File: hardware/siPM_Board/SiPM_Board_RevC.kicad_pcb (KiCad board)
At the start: 4 copper layers, 50.6 x 50.6 mm, 24 parts, among them J1 Conn_02x34_Odd_Even, J2 Conn_02x34_Odd_Even, U1 LM94021, U2 S14161-6050HS-04, U3 S14161-6050HS-04, U4 S14161-6050HS-04, U5 S14161-6050HS-04

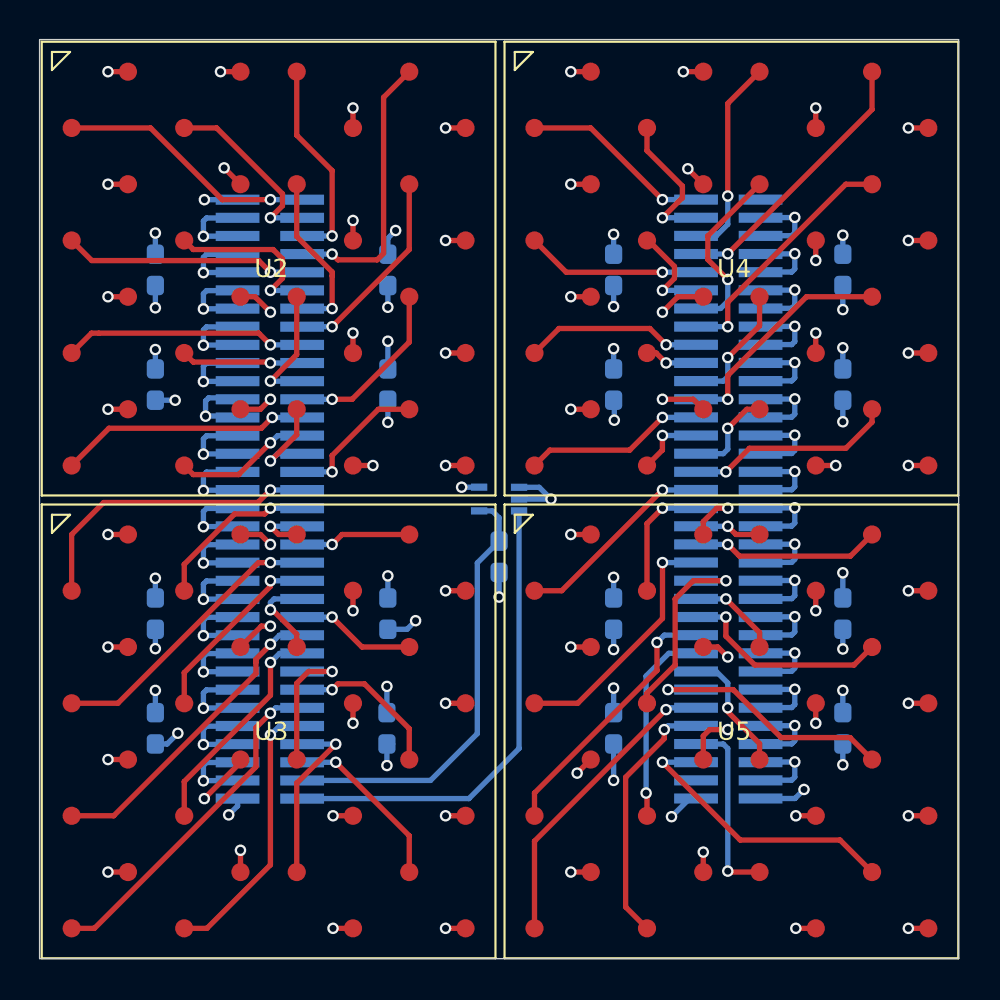
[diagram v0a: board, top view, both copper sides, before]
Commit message: SiPM Board RevC updated
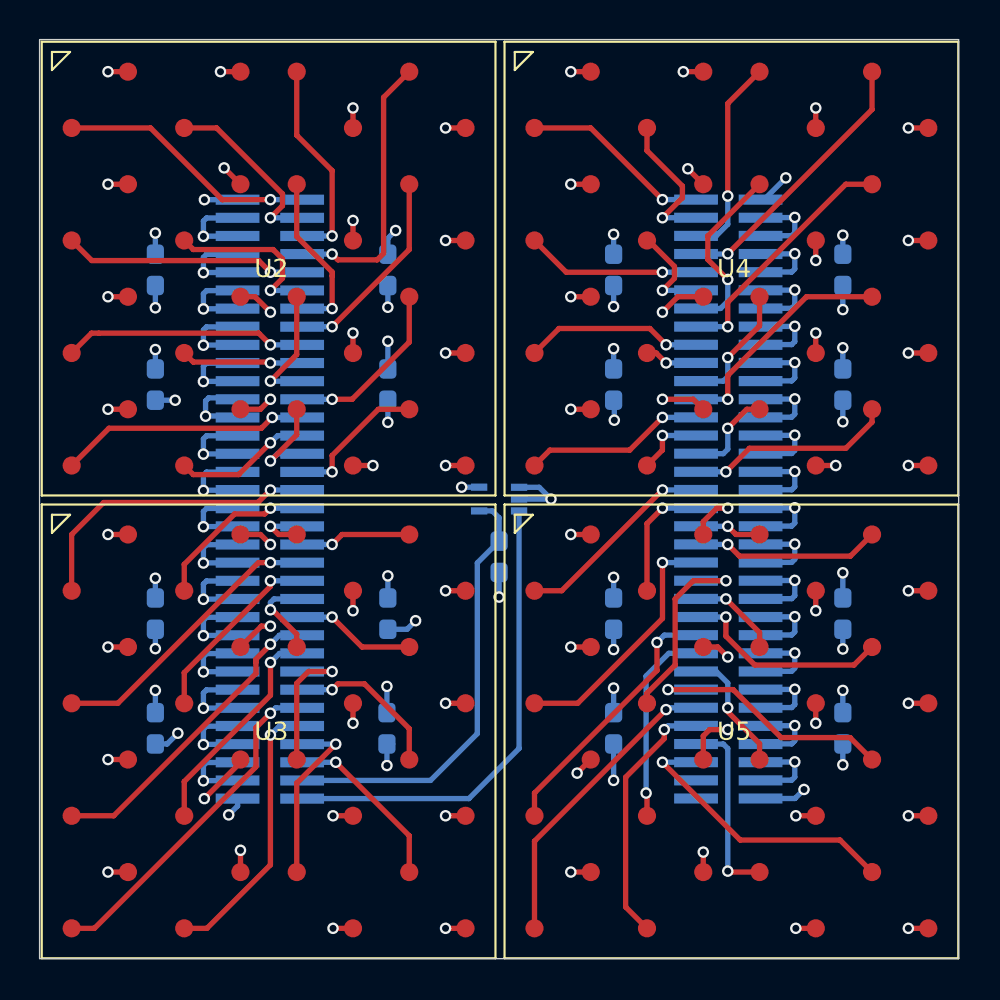
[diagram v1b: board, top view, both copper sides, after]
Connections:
- J2 pad 1: /BIAS4 -> Net-(J2-Pad1)
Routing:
- net /BIAS3: track 25.7 -> 27.6 mm, vias 20 -> 21
- net /BIAS4: track 30.5 -> 28.7 mm, vias 22 -> 21

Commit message: SiPM Board RevC modified
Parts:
- turned J2 to 270 degrees
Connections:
- J2 pad 1: Net-(J2-Pad1) -> /BIAS3
- J2 pad 10: GND -> Net-(J2-Pad10)
- J2 pad 11: Net-(J2-Pad11) -> GND
- J2 pad 12: GND -> Net-(J2-Pad12)
- J2 pad 13: Net-(J2-Pad13) -> GND
- J2 pad 14: GND -> Net-(J2-Pad14)
- J2 pad 15: Net-(J2-Pad15) -> GND
- J2 pad 16: GND -> Net-(J2-Pad16)
- J2 pad 17: Net-(J2-Pad17) -> GND
- J2 pad 18: GND -> Net-(J2-Pad18)
- J2 pad 19: Net-(J2-Pad19) -> GND
- J2 pad 2: /BIAS4 -> Net-(J2-Pad2)
- J2 pad 20: GND -> Net-(J2-Pad20)
- J2 pad 21: Net-(J2-Pad21) -> GND
- J2 pad 22: GND -> Net-(J2-Pad22)
- J2 pad 23: Net-(J2-Pad23) -> GND
- J2 pad 24: GND -> Net-(J2-Pad24)
- J2 pad 25: Net-(J2-Pad25) -> GND
- J2 pad 26: GND -> Net-(J2-Pad26)
- J2 pad 27: Net-(J2-Pad27) -> GND
- J2 pad 28: GND -> Net-(J2-Pad28)
- J2 pad 29: Net-(J2-Pad29) -> GND
- J2 pad 3: Net-(J2-Pad3) -> GND
- J2 pad 30: GND -> Net-(J2-Pad30)
- J2 pad 31: Net-(J2-Pad31) -> GND
- J2 pad 32: GND -> Net-(J2-Pad32)
- J2 pad 33: Net-(J2-Pad33) -> GND
- J2 pad 34: GND -> Net-(J2-Pad34)
- J2 pad 35: Net-(J2-Pad35) -> GND
- J2 pad 36: GND -> Net-(J2-Pad36)
- J2 pad 37: Net-(J2-Pad37) -> GND
- J2 pad 38: GND -> Net-(J2-Pad38)
- J2 pad 39: Net-(J2-Pad39) -> GND
- J2 pad 4: GND -> Net-(J2-Pad4)
- J2 pad 40: GND -> Net-(J2-Pad40)
- J2 pad 41: Net-(J2-Pad41) -> GND
- J2 pad 42: GND -> Net-(J2-Pad42)
- J2 pad 43: Net-(J2-Pad43) -> GND
- J2 pad 44: GND -> Net-(J2-Pad44)
- J2 pad 45: Net-(J2-Pad45) -> GND
- J2 pad 46: GND -> Net-(J2-Pad46)
- J2 pad 47: Net-(J2-Pad47) -> GND
- J2 pad 48: GND -> Net-(J2-Pad48)
- J2 pad 49: Net-(J2-Pad49) -> GND
- J2 pad 5: Net-(J2-Pad5) -> GND
- J2 pad 50: GND -> Net-(J2-Pad50)
- J2 pad 51: Net-(J2-Pad51) -> GND
- J2 pad 52: GND -> Net-(J2-Pad52)
- J2 pad 53: Net-(J2-Pad53) -> GND
- J2 pad 54: GND -> Net-(J2-Pad54)
- J2 pad 55: Net-(J2-Pad55) -> GND
- J2 pad 56: GND -> Net-(J2-Pad56)
- J2 pad 57: Net-(J2-Pad57) -> GND
- J2 pad 58: GND -> Net-(J2-Pad58)
- J2 pad 59: Net-(J2-Pad59) -> GND
- J2 pad 6: GND -> Net-(J2-Pad6)
- J2 pad 60: GND -> Net-(J2-Pad60)
- J2 pad 61: Net-(J2-Pad61) -> GND
- J2 pad 62: GND -> Net-(J2-Pad62)
- J2 pad 63: Net-(J2-Pad63) -> GND
- J2 pad 64: GND -> Net-(J2-Pad64)
- J2 pad 65: Net-(J2-Pad65) -> GND
- J2 pad 66: GND -> Net-(J2-Pad66)
- J2 pad 67: Net-(J2-Pad67) -> /BIAS4
- J2 pad 68: /BIAS3 -> Net-(J2-Pad68)
- J2 pad 7: Net-(J2-Pad7) -> GND
- J2 pad 8: GND -> Net-(J2-Pad8)
- J2 pad 9: Net-(J2-Pad9) -> GND
- U4 pad A2: Net-(J2-Pad67) -> Net-(J2-Pad2)
- U4 pad A4: Net-(J2-Pad59) -> Net-(J2-Pad10)
- U4 pad A6: Net-(J2-Pad51) -> Net-(J2-Pad18)
- U4 pad A8: Net-(J2-Pad43) -> Net-(J2-Pad26)
- U4 pad C2: Net-(J2-Pad65) -> Net-(J2-Pad4)
- U4 pad C4: Net-(J2-Pad57) -> Net-(J2-Pad12)
- U4 pad C6: Net-(J2-Pad49) -> Net-(J2-Pad20)
- U4 pad C8: Net-(J2-Pad41) -> Net-(J2-Pad28)
- U4 pad E1: Net-(J2-Pad63) -> Net-(J2-Pad6)
- U4 pad E3: Net-(J2-Pad55) -> Net-(J2-Pad14)
- U4 pad E5: Net-(J2-Pad47) -> Net-(J2-Pad22)
- U4 pad E7: Net-(J2-Pad39) -> Net-(J2-Pad30)
- U4 pad G1: Net-(J2-Pad61) -> Net-(J2-Pad8)
- U4 pad G3: Net-(J2-Pad53) -> Net-(J2-Pad16)
- U4 pad G5: Net-(J2-Pad45) -> Net-(J2-Pad24)
- U4 pad G7: Net-(J2-Pad37) -> Net-(J2-Pad32)
- U5 pad A2: Net-(J2-Pad35) -> Net-(J2-Pad34)
- U5 pad A4: Net-(J2-Pad27) -> Net-(J2-Pad42)
- U5 pad A6: Net-(J2-Pad19) -> Net-(J2-Pad50)
- U5 pad A8: Net-(J2-Pad11) -> Net-(J2-Pad58)
- U5 pad C2: Net-(J2-Pad33) -> Net-(J2-Pad36)
- U5 pad C4: Net-(J2-Pad25) -> Net-(J2-Pad44)
- U5 pad C6: Net-(J2-Pad17) -> Net-(J2-Pad52)
- U5 pad C8: Net-(J2-Pad9) -> Net-(J2-Pad60)
- U5 pad E1: Net-(J2-Pad31) -> Net-(J2-Pad38)
- U5 pad E3: Net-(J2-Pad23) -> Net-(J2-Pad46)
- U5 pad E5: Net-(J2-Pad15) -> Net-(J2-Pad54)
- U5 pad E7: Net-(J2-Pad7) -> Net-(J2-Pad62)
- U5 pad G1: Net-(J2-Pad29) -> Net-(J2-Pad40)
- U5 pad G3: Net-(J2-Pad21) -> Net-(J2-Pad48)
- U5 pad G5: Net-(J2-Pad13) -> Net-(J2-Pad56)
- U5 pad G7: Net-(J2-Pad5) -> Net-(J2-Pad64)
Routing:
- net Net-(J2-Pad58): track 0.00 -> 16.7 mm, vias 0 -> 1
- net Net-(J2-Pad11): track 16.7 -> 0.00 mm, vias 1 -> 0
- net Net-(J2-Pad64): track 0.00 -> 15.9 mm, vias 0 -> 1
- net Net-(J2-Pad5): track 15.9 -> 0.00 mm, vias 1 -> 0
- net Net-(J2-Pad8): track 0.00 -> 15.1 mm, vias 0 -> 1
- net Net-(J2-Pad61): track 15.1 -> 0.00 mm, vias 1 -> 0
- net Net-(J2-Pad50): track 0.00 -> 14.9 mm, vias 0 -> 1
- net Net-(J2-Pad19): track 14.7 -> 0.00 mm, vias 1 -> 0
- net Net-(J2-Pad56): track 0.00 -> 14.4 mm, vias 0 -> 1
- net Net-(J2-Pad13): track 14.4 -> 0.00 mm, vias 1 -> 0
- net Net-(J2-Pad60): track 0.00 -> 14.2 mm, vias 0 -> 1
- net Net-(J2-Pad9): track 14.2 -> 0.00 mm, vias 1 -> 0
- net Net-(J2-Pad42): track 0.00 -> 14.1 mm, vias 0 -> 1
- net Net-(J2-Pad27): track 13.9 -> 0.00 mm, vias 1 -> 0
- net Net-(J2-Pad53): track 13.7 -> 0.00 mm, vias 1 -> 0
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
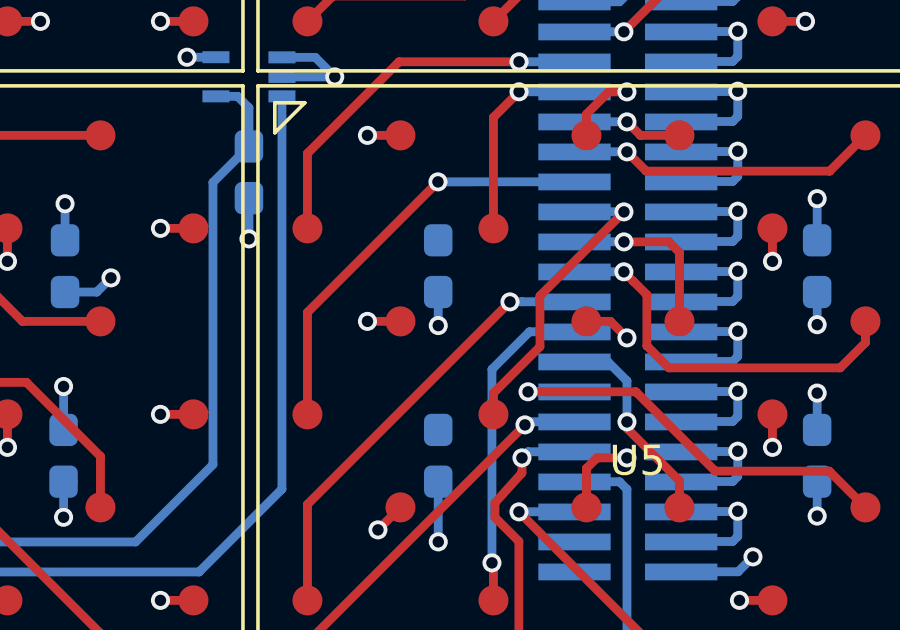
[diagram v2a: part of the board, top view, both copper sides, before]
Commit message: SiPM Board RevC layout modified
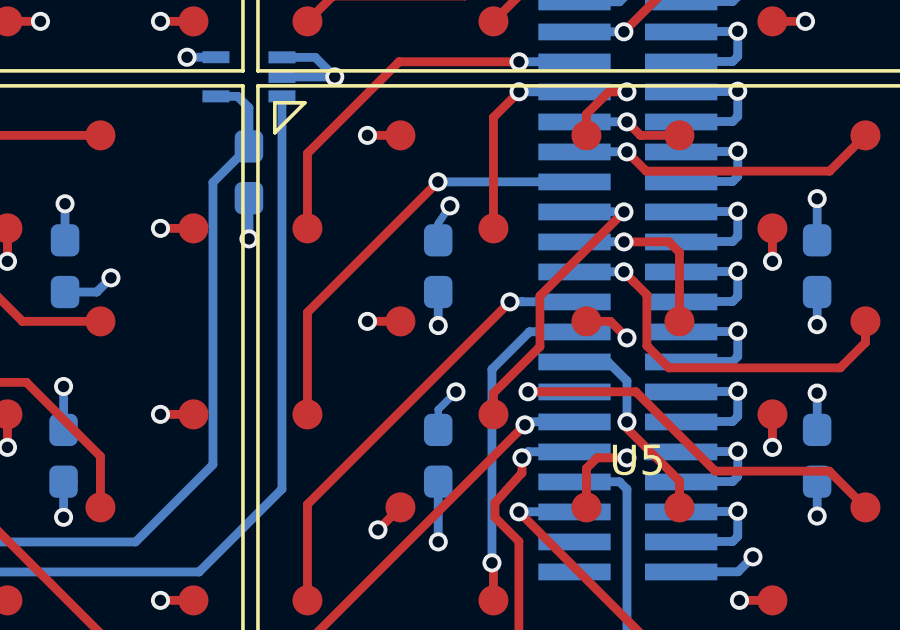
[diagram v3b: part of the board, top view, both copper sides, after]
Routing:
- net /BIAS4: track 26.2 -> 29.0 mm, vias 19 -> 21

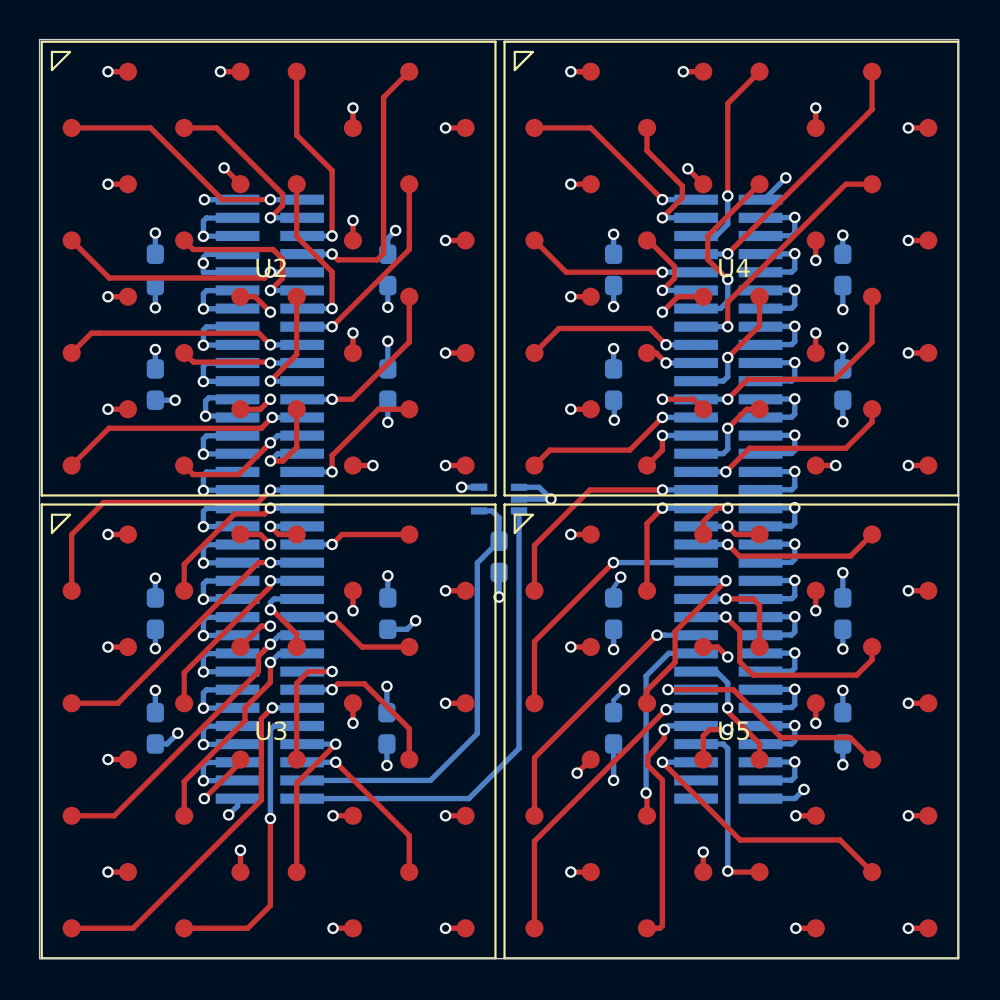
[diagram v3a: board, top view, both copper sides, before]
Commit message: SiPM Board Layout edited
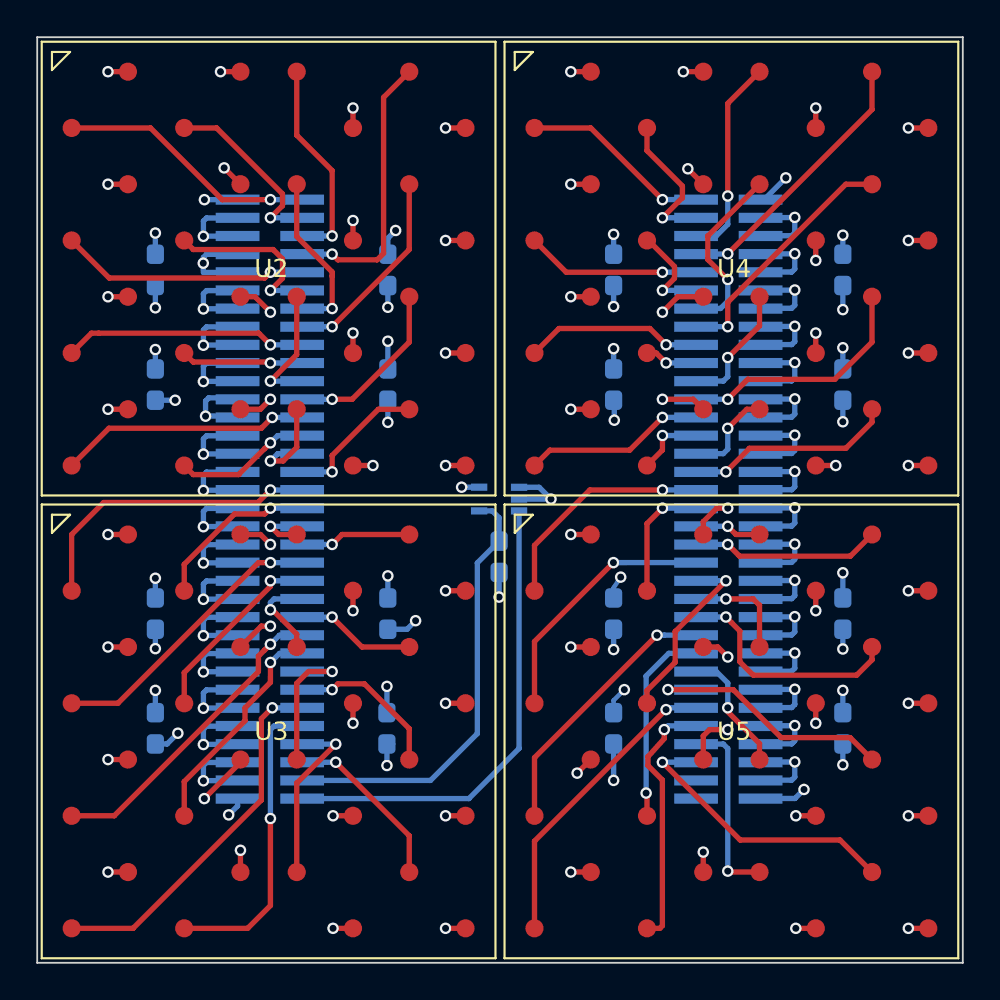
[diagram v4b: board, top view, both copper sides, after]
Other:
- board size 50.6 x 50.6 mm -> 51 x 51 mm

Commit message: SiPM RevC modified
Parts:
- moved J1 0.12 mm to (137.2, 100.0)
- moved J2 0.12 mm to (162.8, 100.0)
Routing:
- net Net-(J2-Pad64): track 15.9 -> 13.4 mm
- net Net-(J2-Pad6): track 11.1 -> 12.4 mm
- net Net-(J2-Pad62): track 10.4 -> 9.39 mm
- net Net-(J2-Pad4): track 8.07 -> 7.16 mm
- net Net-(J1-Pad45): track 4.97 -> 5.73 mm
- net /BIAS4: track 29.0 -> 29.6 mm
- net Net-(J2-Pad12): track 5.56 -> 5.04 mm
- net Net-(J2-Pad2): track 10.5 -> 11.0 mm
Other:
- board size 51 x 51 mm -> 50.8 x 50.8 mm

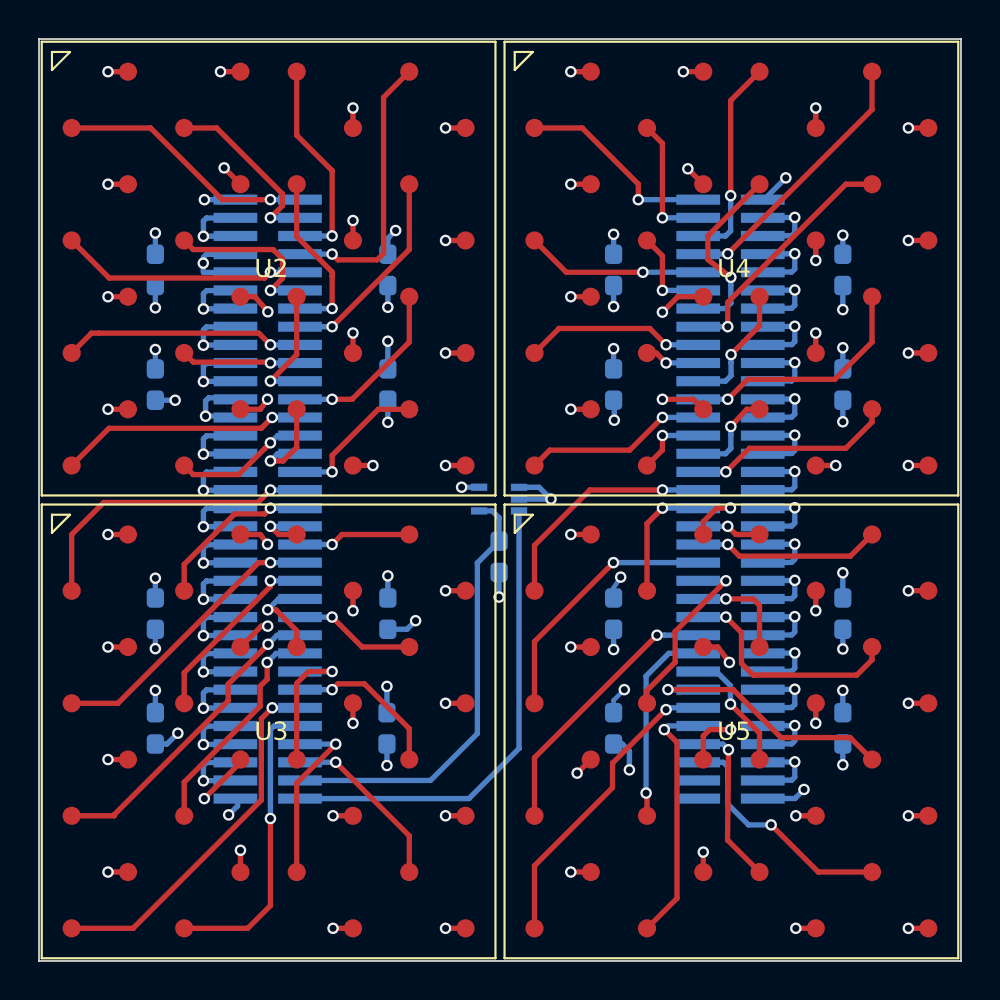
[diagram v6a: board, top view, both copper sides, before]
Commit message: Branch to add PEM nuts to SiPM board
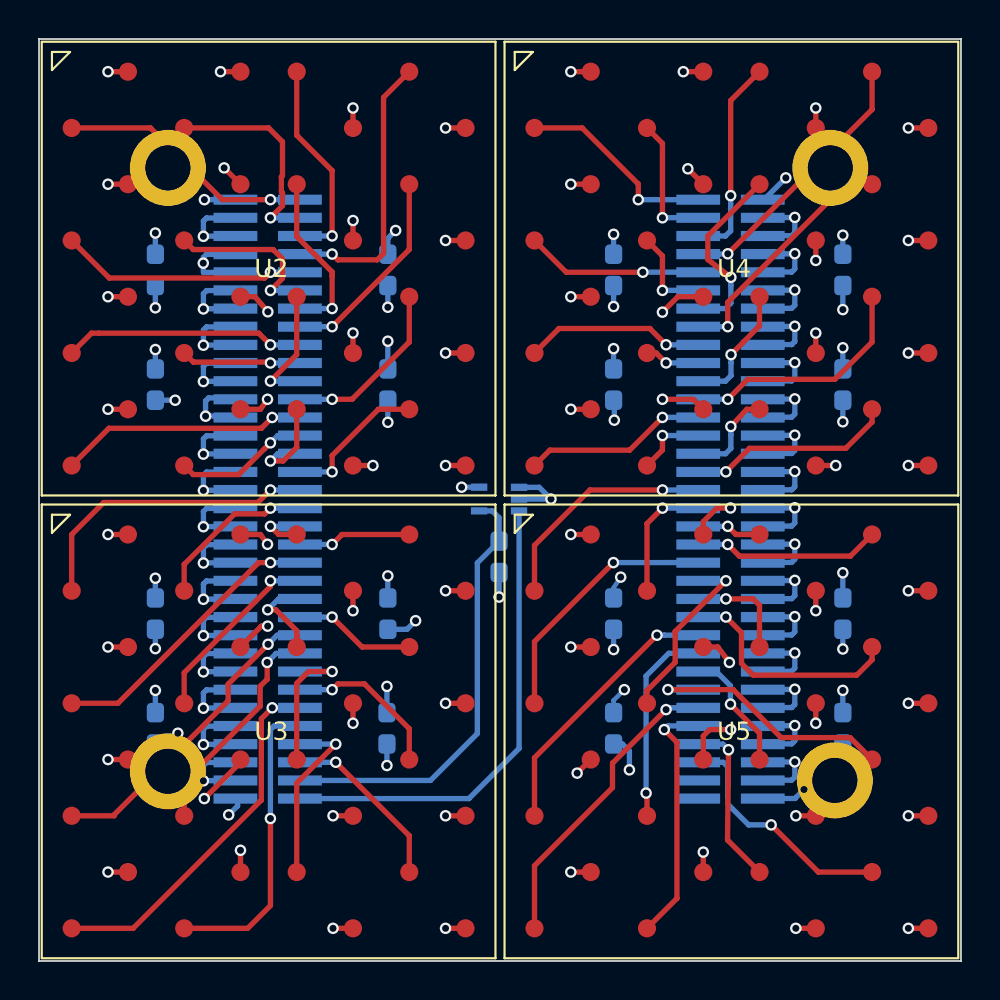
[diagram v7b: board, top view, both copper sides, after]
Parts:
- added H1: MountingHole, Arich_SiPM_Footprints:SMTSO-nut-0-80, B.Cu at (131.8, 81.8)
- added H2: MountingHole, Arich_SiPM_Footprints:SMTSO-nut-0-80, B.Cu at (168.2, 81.8)
- added H3: MountingHole, Arich_SiPM_Footprints:SMTSO-nut-0-80, B.Cu at (131.8, 115.0)
- added H4: MountingHole, Arich_SiPM_Footprints:SMTSO-nut-0-80, B.Cu at (168.5, 115.5)
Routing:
- net Net-(J1-Pad3): track 10.3 -> 12.0 mm

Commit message: PEM nuts
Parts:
- moved C6 2.32 mm to (129.4, 111.0)
- moved C17 2.18 mm to (170.8, 111.5)
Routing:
- net GND: track 182.7 -> 173.8 mm, vias 51 -> 49
- net Net-(J2-Pad8): track 15.1 -> 20.3 mm, vias 1 -> 3
- net Net-(J1-Pad1): track 15.0 -> 17.0 mm
- net /BIAS4: track 29.6 -> 27.6 mm
- net Net-(J2-Pad16): track 13.7 -> 15.4 mm
- net /BIAS2: track 27.2 -> 28.6 mm, vias 21 -> 20
- net Net-(J1-Pad49): track 17.4 -> 18.5 mm
- net Net-(J1-Pad57): track 20.4 -> 21.1 mm
- net Net-(J1-Pad51): track 12.4 -> 13.0 mm
